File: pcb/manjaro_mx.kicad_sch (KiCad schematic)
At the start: 103 parts, among them J1 AudioJack3, J2 MJ-4PP-9, SW1 SW_Push, SW10 SW_Push, SW11 SW_Push, SW12 SW_Push, SW13 SW_Push, SW14 SW_Push, SW15 SW_Push, SW16 SW_Push, SW17 SW_Push, SW18 SW_Push, SW19 SW_Push, SW2 SW_Push, SW20 SW_Push, SW21 SW_Push, SW22 SW_Push, SW23 SW_Push, SW24 SW_Push, SW3 SW_Push, SW4 SW_Push, SW5 SW_Push, SW6 SW_Push, SW7 SW_Push, SW8 SW_Push, SW9 SW_Push, U1 nice_nano

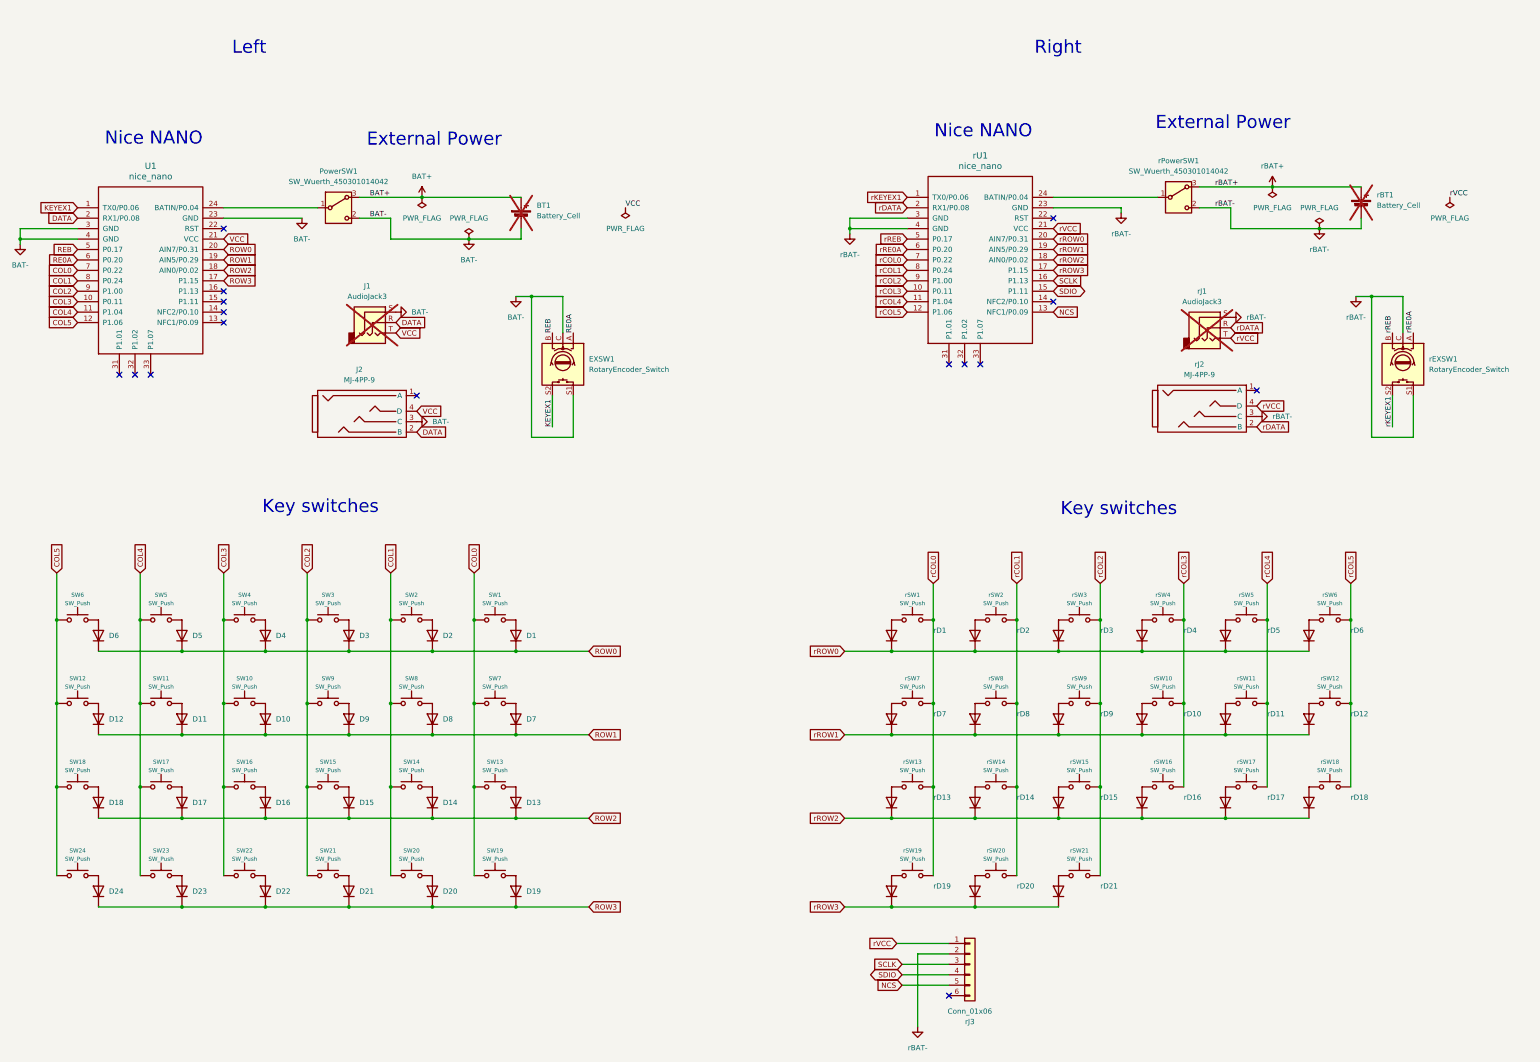
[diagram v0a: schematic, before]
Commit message: [base] layout 7x4 with RP2040 MCU
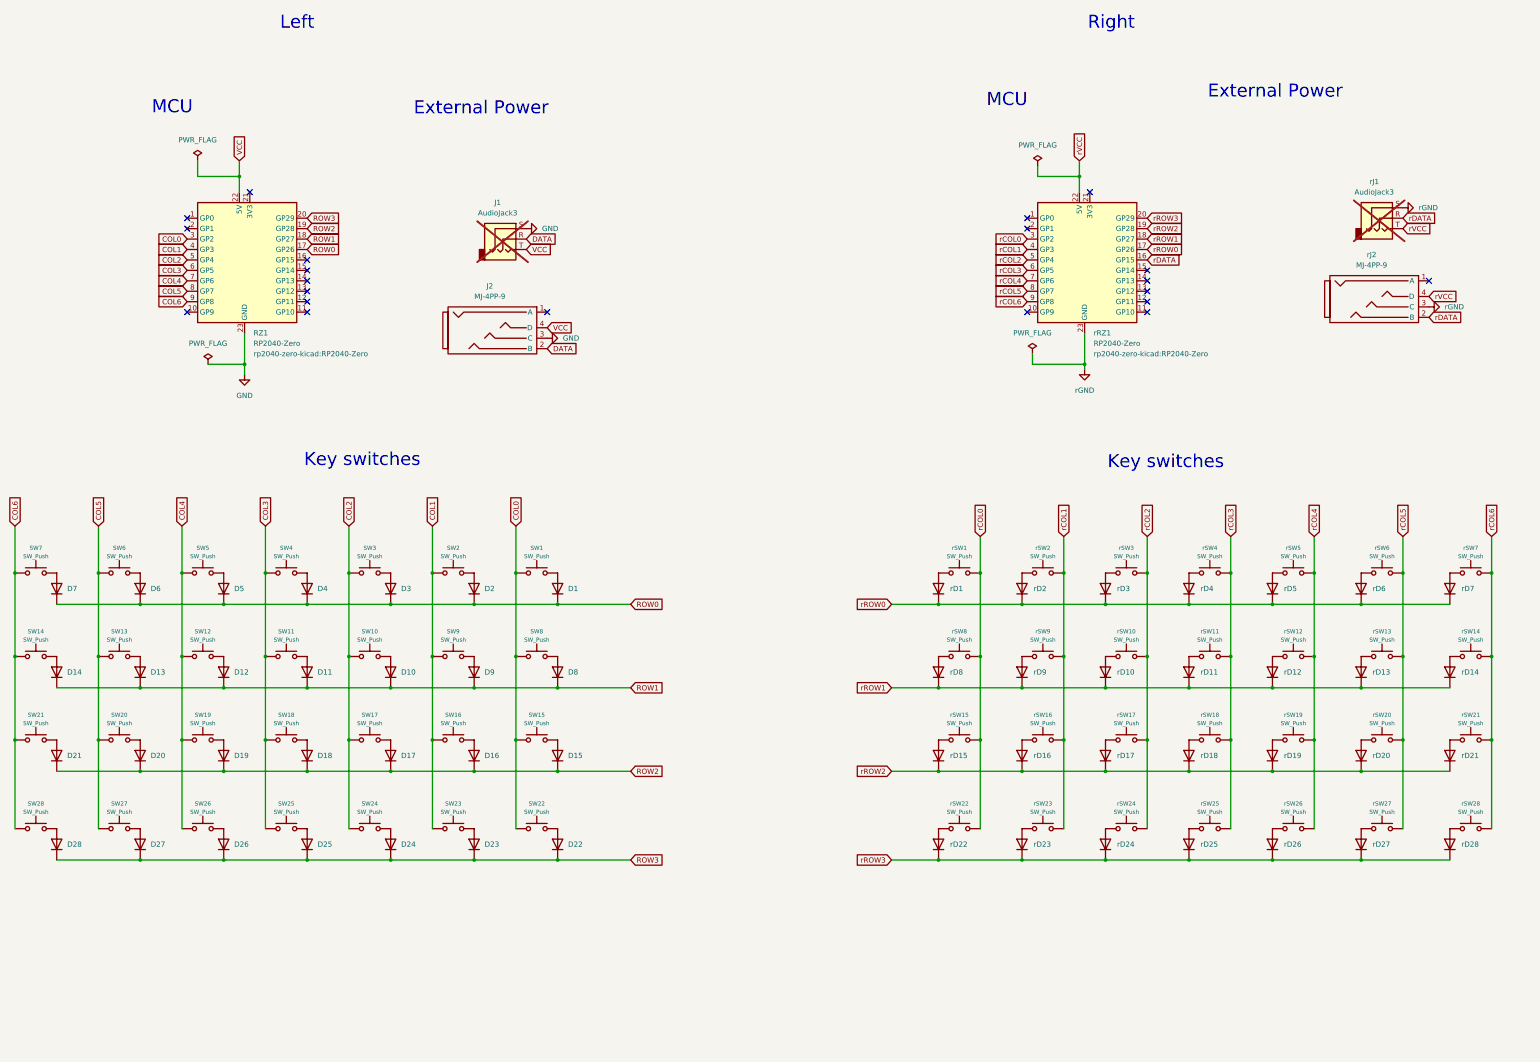
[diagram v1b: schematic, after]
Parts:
- removed BT1, rBT1: Battery_Cell, Connector_JST:JST_PH_S2B-PH-K_1x02_P2.00mm_Horizontal, symbol Device:Battery_Cell
- removed D12, D6, rD12, rD18, rD6: 1N4148WT, Keebio-Parts:D_SOD-323, symbol Diode:1N4148WT
- removed EXSW1, rEXSW1: RotaryEncoder_Switch, Keebio-Parts:RotaryEncoder_EC11, symbol Device:RotaryEncoder_Switch
- removed PowerSW1, rPowerSW1: SW_Wuerth_450301014042, Button_Switch_THT:SW_Slide-03_Wuerth-WS-SLTV_10x2.5x6.4_P2.54mm, symbol Switch:SW_Wuerth_450301014042
- removed SW12, SW6, rSW12, rSW18, rSW6: SW_Push, kbd:keyswitch_cherrymx_hotswap_1u, symbol Switch:SW_Push
- removed U1, rU1: nice_nano, nice-nano-kicad:nice_nano, symbol nice_nano:nice_nano
- removed rJ3: Conn_01x06, Connector_PinHeader_2.54mm:PinHeader_1x06_P2.54mm_Vertical, symbol Connector_Generic:Conn_01x06
- added D19, D20, D25, D26, D27, D28, rD19, rD20, rD21, rD22, rD23, rD24, rD25, rD26, rD27, rD28: 1N4148WT, Keebio-Parts:D_SOD-323, symbol Diode:1N4148WT
- added RZ1, rRZ1: RP2040-Zero, rp2040-zero-kicad:RP2040-Zero, symbol rp2040-zero:RP2040-Zero
- added SW19, SW20, SW25, SW26, SW27, SW28, rSW19, rSW20, rSW21, rSW25, rSW26, rSW27, rSW28: SW_Push, kbd:keyswitch_cherrymx_hotswap_1u, symbol Switch:SW_Push
- added rSW22, rSW23, rSW24: SW_Push, kbd:keyswitch_choc12_hotswap_1u, symbol Switch:SW_Push
- SW22, SW23, SW24: footprint kbd:keyswitch_cherrymx_hotswap_1u -> kbd:keyswitch_choc12_hotswap_1u
- renumbered D11 to D10, D13 to D11, D14 to D12, D15 to D13, D16 to D14, D17 to D15, D19 to D16, D20 to D17, D7 to D6, D8 to D7, D9 to D8, D10 to D9, SW11 to SW10, SW13 to SW11, SW14 to SW12, SW15 to SW13, SW16 to SW14, SW17 to SW15, SW19 to SW16, SW20 to SW17, SW7 to SW6, SW8 to SW7, SW9 to SW8, SW10 to SW9, rD11 to rD10, rD13 to rD11, rD14 to rD12, rD15 to rD13, rD16 to rD14, rD17 to rD15, rD19 to rD16, rD20 to rD17, rD21 to rD18, rD7 to rD6, rD8 to rD7, rD9 to rD8, rD10 to rD9, rSW11 to rSW10, rSW13 to rSW11, rSW14 to rSW12, rSW15 to rSW13, rSW16 to rSW14, rSW17 to rSW15, rSW19 to rSW16, rSW20 to rSW17, rSW21 to rSW18, rSW7 to rSW6, rSW8 to rSW7, rSW9 to rSW8, rSW10 to rSW9
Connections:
- net COL0: now also SW15.1, SW22.1, SW8.1, RZ1.3 (GP2); no longer SW11.1, SW16.1, SW6.1
- net COL1: now also SW16.1, SW23.1, SW9.1, RZ1.4 (GP3); no longer SW12.1, SW17.1, SW7.1
- net COL2: now also SW10.1, SW17.1, SW24.1, RZ1.5 (GP4); no longer SW13.1, SW21.1, SW8.1
- net COL3: now also SW11.1, SW18.1, RZ1.6 (GP5), SW25.1; no longer SW14.1, SW22.1, SW9.1
- net COL4: now also SW12.1, RZ1.7 (GP6), SW19.1, SW26.1; no longer SW10.1, SW15.1, SW23.1
- net COL5: now also SW13.1, SW6.1, RZ1.8 (GP7), SW20.1, SW27.1; no longer SW18.1, SW24.1
- net ROW0: now also D6.1 (K), D7.1 (K), RZ1.17 (GP26)
- net ROW1: now also D11.1 (K), D12.1 (K), D13.1 (K), D14.1 (K), RZ1.18 (GP27); no longer D6.1 (K), D7.1 (K)
- net ROW2: now also D16.1 (K), D17.1 (K), D21.1 (K), D19.1 (K), D20.1 (K), RZ1.19 (GP28); no longer D11.1 (K), D12.1 (K), D13.1 (K), D14.1 (K)
- net ROW3: now also D25.1 (K), D26.1 (K), D27.1 (K), D28.1 (K), RZ1.20 (GP29); no longer D16.1 (K), D17.1 (K), D21.1 (K)
- net VCC: now also RZ1.22 (5V)
- net rCOL0: now also rSW15.2, rSW8.2, rRZ1.3 (GP2), rSW22.2; no longer rSW11.2, rSW16.2, rSW6.2
- net rCOL1: now also rSW16.2, rSW9.2, rRZ1.4 (GP3), rSW23.2; no longer rSW12.2, rSW17.2, rSW7.2
- net rCOL2: now also rSW10.2, rSW17.2, rRZ1.5 (GP4), rSW24.2; no longer rSW13.2, rSW18.2, rSW8.2
- net rCOL3: now also rSW11.2, rSW18.2, rRZ1.6 (GP5), rSW25.2; no longer rSW14.2, rSW9.2
- net rCOL4: now also rSW12.2, rRZ1.7 (GP6), rSW19.2, rSW26.2; no longer rSW10.2, rSW15.2
- net rCOL5: now also rSW13.2, rSW6.2, rRZ1.8 (GP7), rSW20.2, rSW27.2
- net rDATA: now also rRZ1.16 (GP15)
- net rROW0: now also rD6.1 (K), rD7.1 (K), rRZ1.17 (GP26)
- net rROW1: now also rD11.1 (K), rD12.1 (K), rD13.1 (K), rD14.1 (K), rRZ1.18 (GP27); no longer rD6.1 (K), rD7.1 (K)
- net rROW2: now also rD16.1 (K), rD17.1 (K), rD18.1 (K), rD19.1 (K), rD20.1 (K), rD21.1 (K), rRZ1.19 (GP28); no longer rD11.1 (K), rD12.1 (K), rD13.1 (K), rD14.1 (K)
- net rROW3: now also rD22.1 (K), rD23.1 (K), rD24.1 (K), rD25.1 (K), rD26.1 (K), rD27.1 (K), rD28.1 (K), rRZ1.20 (GP29); no longer rD16.1 (K), rD17.1 (K), rD18.1 (K)
- net rVCC: now also rRZ1.22 (5V)
- net BAT- renamed GND
- net GND: now also RZ1.23 (GND)
- net rBAT- renamed rGND
- net rGND: now also rRZ1.23 (GND)
- new net: D26.2 (A), SW26.2
- new net: D28.2 (A), SW28.2
- new net: rD26.2 (A), rSW26.1
- new net: rD21.2 (A), rSW21.1
- new net: rD25.2 (A), rSW25.1
- new net: D19.2 (A), SW19.2
- new net: rD22.2 (A), rSW22.1
- new net: rD27.2 (A), rSW27.1
- new net: rD20.2 (A), rSW20.1
- new net: rD28.2 (A), rSW28.1
- new net: D25.2 (A), SW25.2
- new net: rD19.2 (A), rSW19.1
- new net: rD24.2 (A), rSW24.1
- new net: D20.2 (A), SW20.2
- new net: rD23.2 (A), rSW23.1
- new net: D27.2 (A), SW27.2
- new net COL6: RZ1.9 (GP8), SW14.1, SW21.1, SW28.1, SW7.1
- new net rCOL6: rRZ1.9 (GP8), rSW14.2, rSW21.2, rSW28.2, rSW7.2
- no-connect marks 16 -> 21
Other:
- note added: "MCU"
- note removed: "Nice NANO"
- moved on the sheet: D1, D10, D11, D12, D13, D14, D15, D16, D17, D2, D21, D22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
